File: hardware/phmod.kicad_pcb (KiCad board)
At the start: 4 copper layers, 100 x 100 mm, 234 parts, among them J1001 SMA, J1002 SMA, J1003 SMA, J1004 SMA, J101 USB-C, J201 SMA, J202 SMA, J301 SMA, J302 SMA, J303 SMA, J304 SMA, J401 SMA, J402 VM in, J403 coil, J501 SMA, J502 SMA, J503 SMA, J504 SMA, J505 Pmod, J601 SMA, J602 SMA, J701 SMA, J702 SMA, J703 SMA, J704 SMA, J801 SMA, J802 SMA, J803 SMA, J804 SMA, J901 SMA, Q1001 AO3401A, Q1002 2N7002, Q1003 AO3401A, Q1004 AO3400A, Q301 AO3401A, Q401 AO3401A, Q501 AO3401A, Q601 AO3401A, Q701 AO3401A, Q801 AO3401A, Q901 AO3401A, Q902 MMBT3904, SW1001 ON, SW301 ON, SW401 ON, SW501 ON, SW601 ON, SW701 ON, SW801 ON, SW802 DIP4, SW901 ON, U1001 OPA810, U1002 OPA810, U101 TPS65131, U102 LM2664, U201 THS3491, U301 OPA847, U401 DRV8876, U402 OPA810, U501 LMH6629, U502 LMH6629, U601 OPA810, U701 OPA810, U702 OPA810, U901 TPS22917, U902 LMH6629

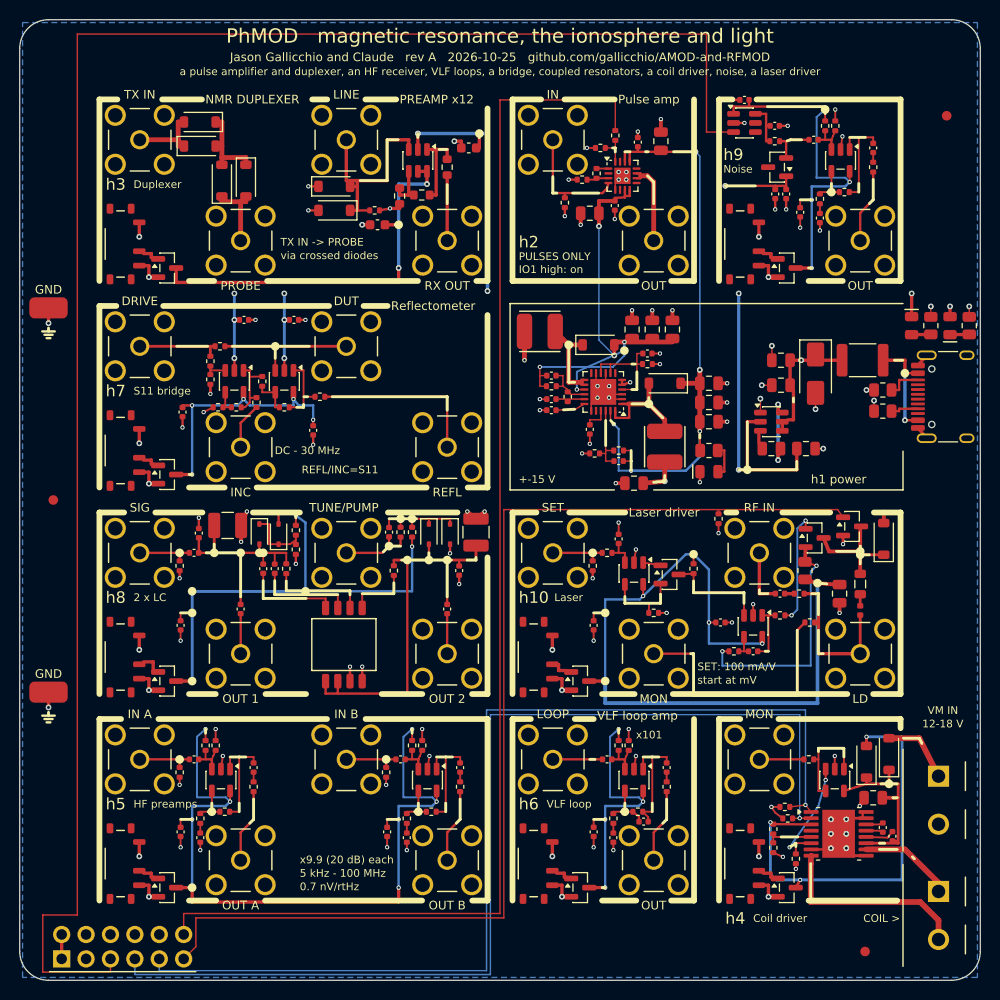
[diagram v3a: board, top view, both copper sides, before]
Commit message: Pre-order checks from CLAUDE_PCB.md's new lessons (Prompt 21): the KF301 terminals turned for their wire openings (CPL +180, body 3.7 / 4.0, a wire-face check), four oversold parts swapped (27R, 6.8k, 220n, OPA847IDBVT at its own +180), fourteen vias moved out of SMD pads (check_layout.py gates it and RF detours), 200-250 mW terminations, assembly drawings from Fab and silk fitted to Letter (fit_pdf.py from CostasLink), the stock gate on JLCPCB's free count, electrolytics in the rotation check, the RF gates surveyed (rf_extract.py, rf_survey.py) and written into the DOA lists; all nine boards rebuilt: ERC 0, DRC 0, every check
Co-Authored-By: Claude Opus 5.5 <noreply@anthropic.com>
Claude-Session: https://claude.ai/code/session_01RKeoKvFFzjk3cEBLCXXHnB
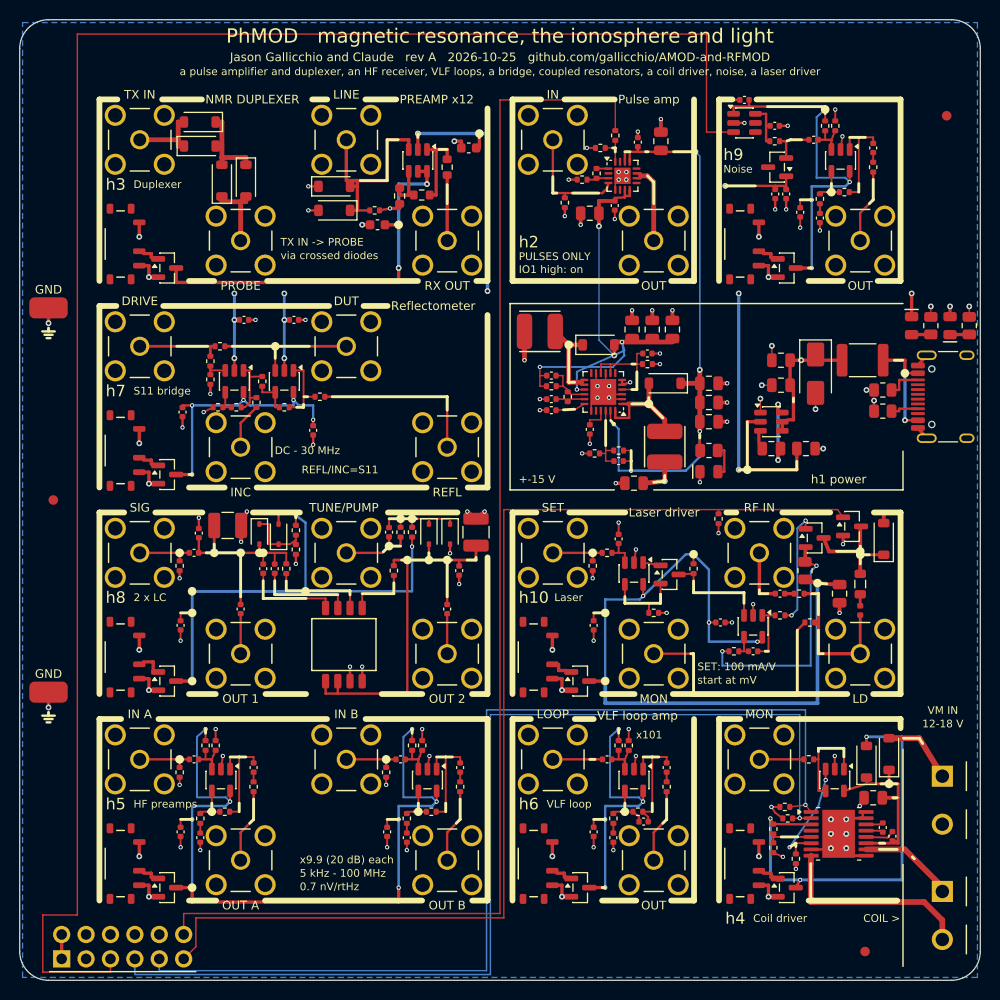
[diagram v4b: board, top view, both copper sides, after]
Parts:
- moved J402 0.40 mm to (96.0, 81.2)
- moved J403 0.40 mm to (96.0, 93.2)
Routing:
- net /h4_VS: track 44.1 -> 44.8 mm
